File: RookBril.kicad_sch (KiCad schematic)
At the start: 29 parts, among them J2 IR_SENSOR0_PINS, J3 IR_SENSOR1_PINS, J4 IR_SENSOR2_PINS, J5 IR_SENSOR3_PINS, J6 LOW-BAT_LED_CONN, J7 PDLC_JST_PINS, U1 VNH7070ASTR

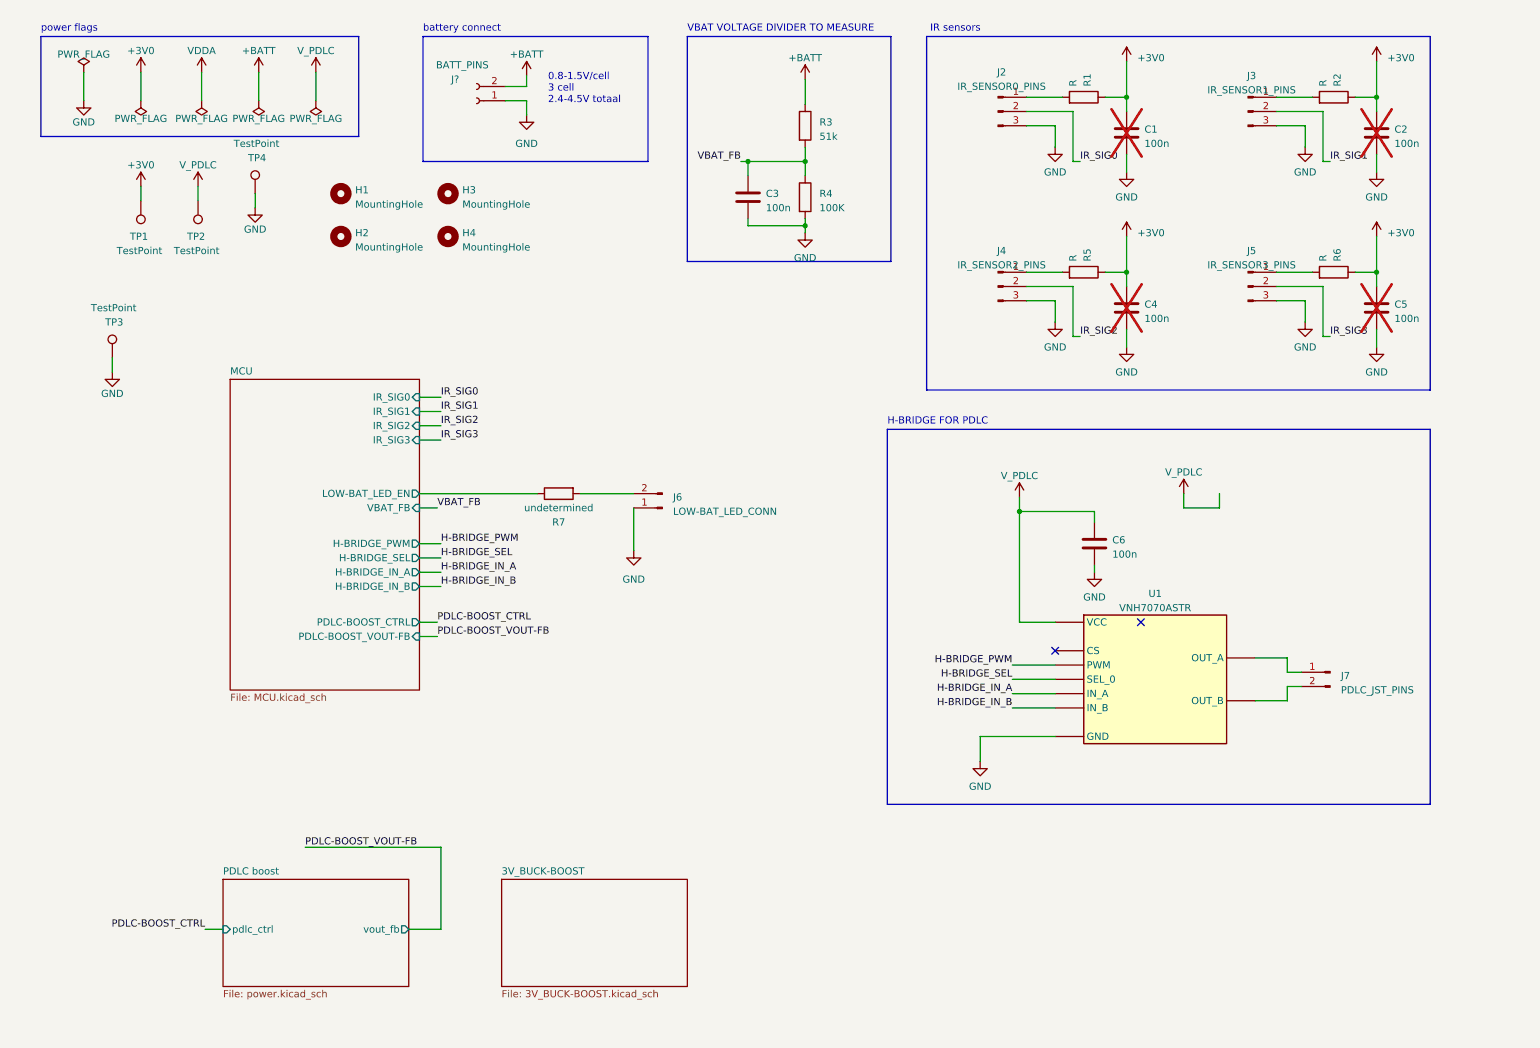
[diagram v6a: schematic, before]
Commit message: PCBv2.01
Eerste versie van de tweede versie van de pcb prototype.
Nieuwe PDLC voeding, extra pinnen beschikbaar voor GUI inclusief voeding pinnen.
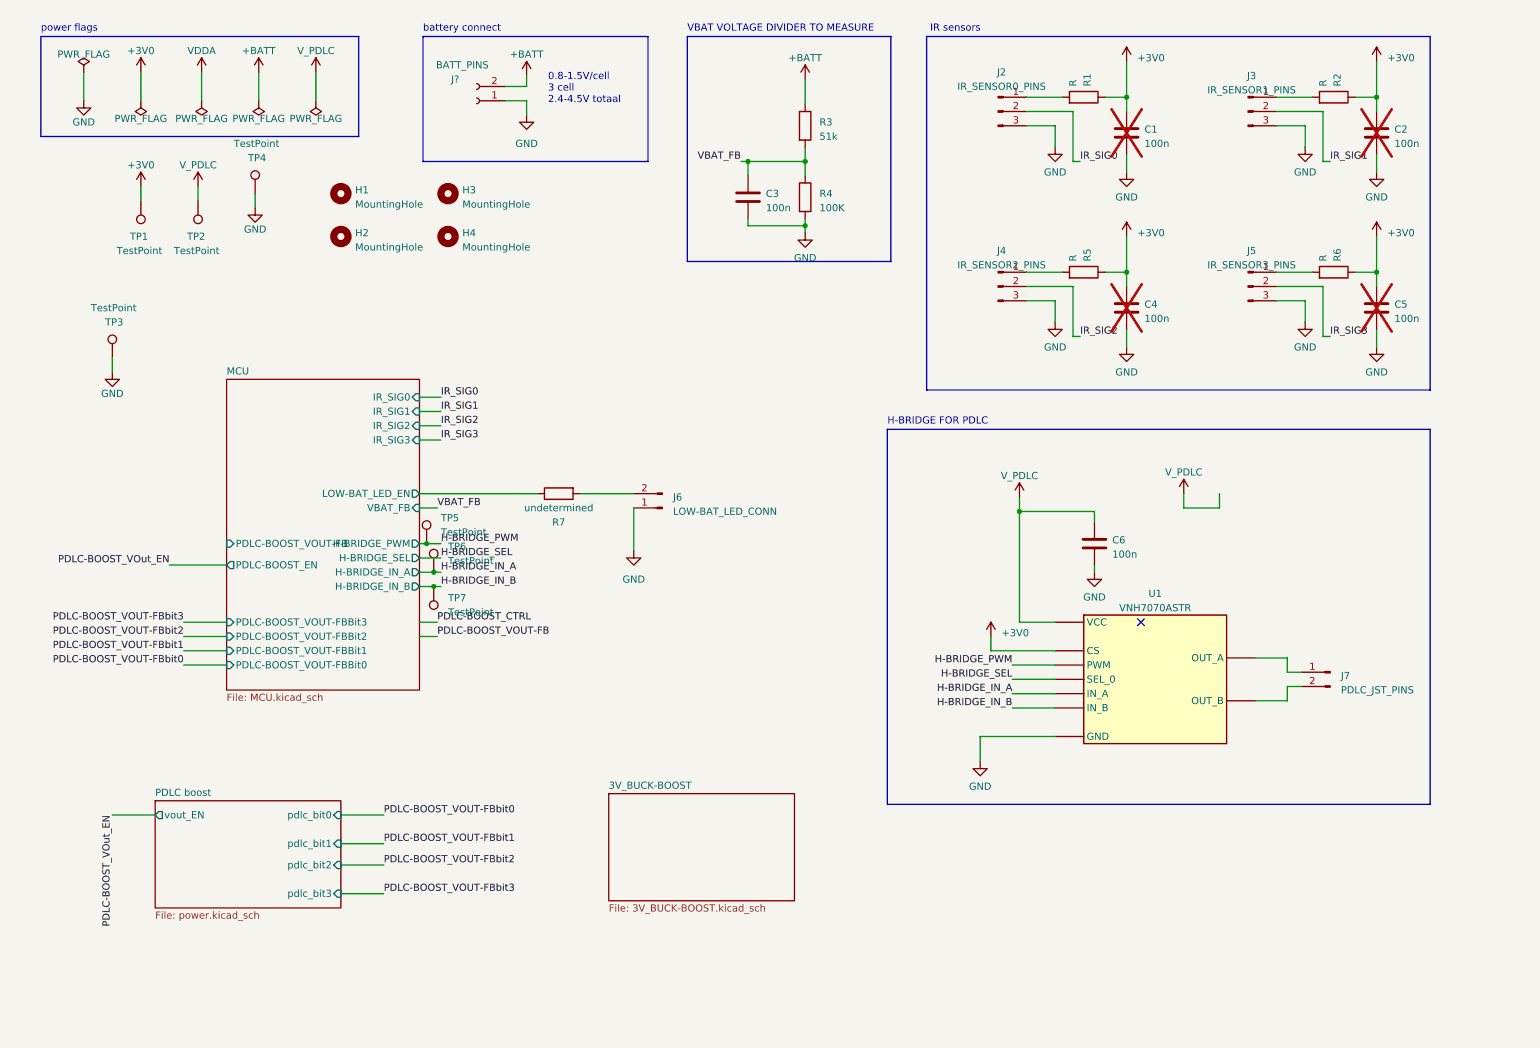
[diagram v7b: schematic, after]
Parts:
- added TP5, TP6, TP7: TestPoint, TestPoint:TestPoint_Pad_D1.0mm, symbol Connector:TestPoint
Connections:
- net +3V0: now also U1.13 (CS)
- net H-BRIDGE_IN_A: now also TP6.1
- net H-BRIDGE_IN_B: now also TP7.1
- net H-BRIDGE_PWM: now also TP5.1
- no-connect marks 2 -> 1
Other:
- sheet MCU ports: added PDLC-BOOST_EN, PDLC-BOOST_VOUT-FBBit0, PDLC-BOOST_VOUT-FBBit1, PDLC-BOOST_VOUT-FBBit2, PDLC-BOOST_VOUT-FBBit3; removed PDLC-BOOST_CTRL
- sheet PDLC boost ports: added pdlc_bit0, pdlc_bit1, pdlc_bit2, pdlc_bit3, vout_EN; removed pdlc_ctrl, vout_fb

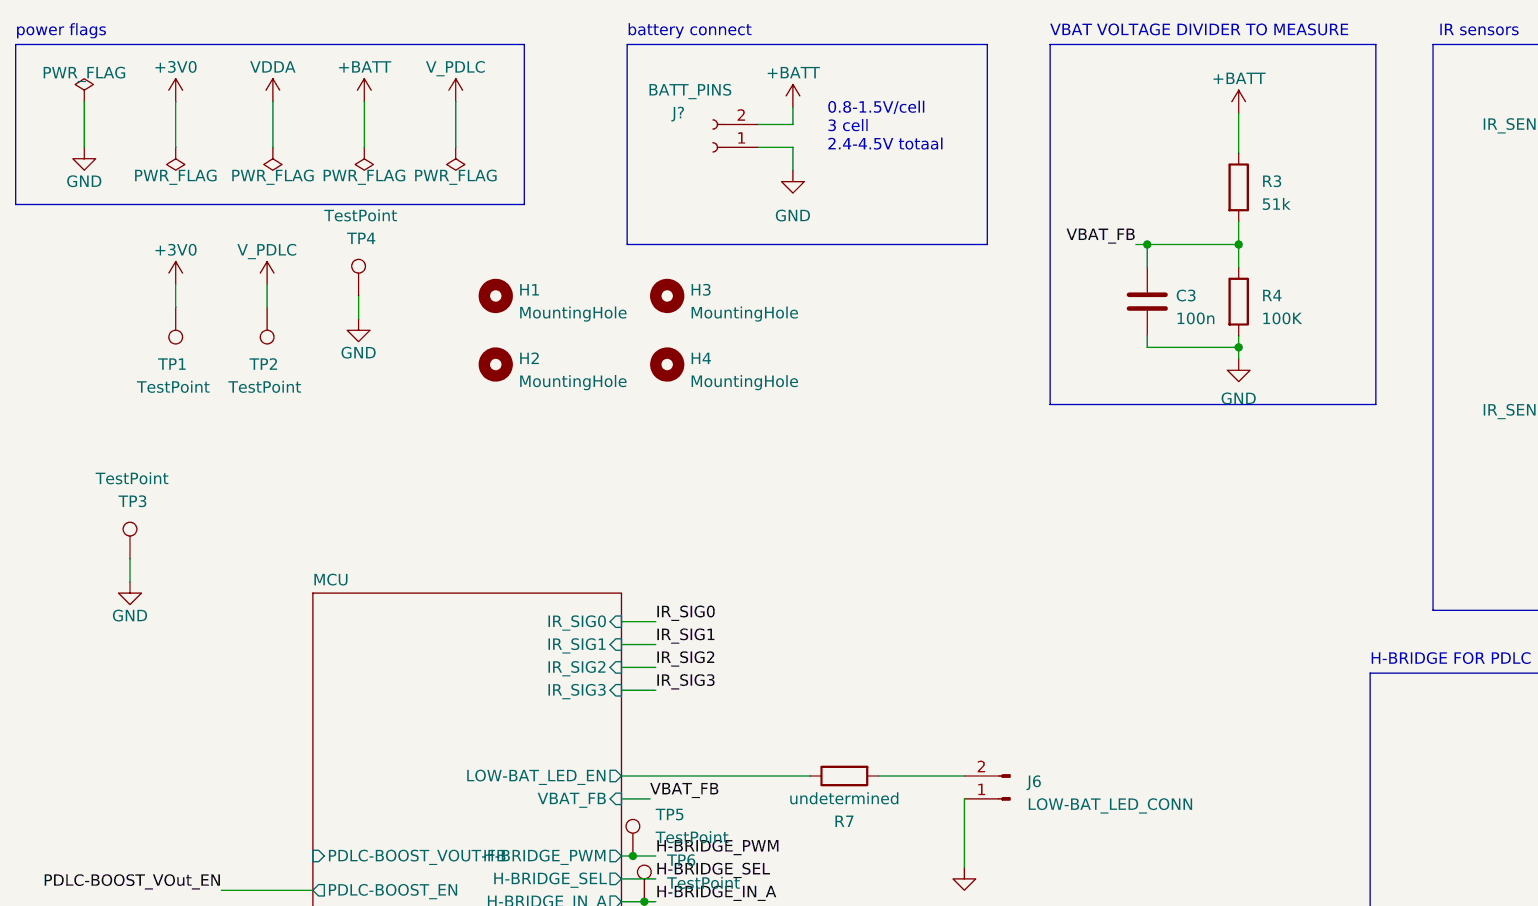
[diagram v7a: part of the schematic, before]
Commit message: PCBv2.02
Toepassingen van wouters feedback.
Condensatoren beter geplaatst bij pdlc, mosfet toegevoegd bij fb bat, extra vias toegevoegd en traces verschoven voor betere GND plane connecties
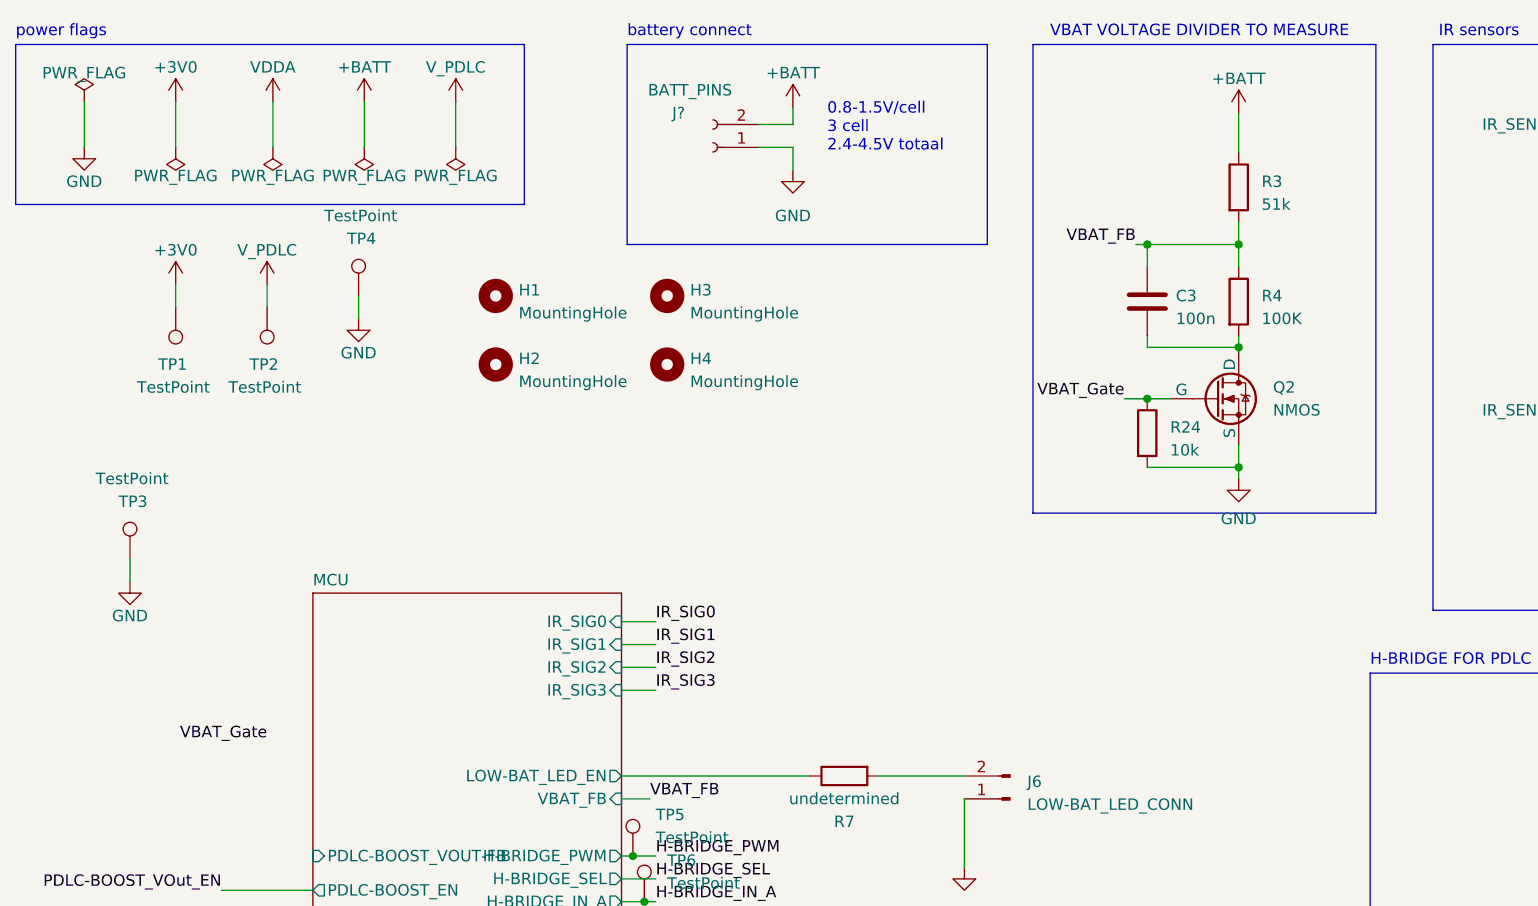
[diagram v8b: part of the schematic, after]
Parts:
- added Q2: NMOS, Package_TO_SOT_SMD:SOT-23, symbol Simulation_SPICE:NMOS
- added R24: 10k, Resistor_SMD:R_0805_2012Metric_Pad1.20x1.40mm_HandSolder, symbol Device:R
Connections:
- net GND: now also Q2.3 (S), R24.2; no longer C3.2, R4.2
- new net: C3.2, Q2.1 (D), R4.2
- new net VBAT_Gate: Q2.2 (G), R24.1
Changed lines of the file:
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@@
   (junction (at 151.13 51.435) (diameter 0) (color 0 0 0 0)
   )
+  (junction (at 140.97 57.15) (diameter 0) (color 0 0 0 0)
+  )
   (junction (at 140.97 40.005) (diameter 0) (color 0 0 0 0)
   )
@@
   )
   (junction (at 85.09 115.57) (diameter 0) (color 0 0 0 0)
+  )
+  (junction (at 151.13 64.77) (diameter 0) (color 0 0 0 0)
   )
   (junction (at 85.09 113.03) (diameter 0) (color 0 0 0 0)
@@
     (stroke (width 0) (type default))
   )
+  (wire (pts (xy 138.43 57.15) (xy 140.97 57.15))
+    (stroke (width 0) (type default))
+  )
   (wire (pts (xy 243.205 40.005) (xy 244.475 40.005))
     (stroke (width 0) (type default))
@@
     (stroke (width 0) (type default))
   )
+  (wire (pts (xy 140.97 57.15) (xy 143.51 57.15))
+    (stroke (width 0) (type default))
+  )
   (wire (pts (xy 243.205 31.115) (xy 234.95 31.115))
     (stroke (width 0) (type default))
@@
     (stroke (width 0) (type default))
   )
+  (wire (pts (xy 151.13 64.77) (xy 151.13 62.23))
+    (stroke (width 0) (type default))
+  )
   (wire (pts (xy 224.79 101.6) (xy 224.79 99.06))
     (stroke (width 0) (type default))
@@
     (stroke (width 0) (type default))
   )
+  (wire (pts (xy 140.97 64.77) (xy 151.13 64.77))
+    (stroke (width 0) (type default))
+  )
   (wire (pts (xy 184.15 124.46) (xy 184.15 127))
     (stroke (width 0) (type default))
@@
     (stroke (width 0) (type default))
   )
-  (wire (pts (xy 151.13 52.705) (xy 151.13 51.435))
+  (wire (pts (xy 151.13 66.04) (xy 151.13 64.77))
     (stroke (width 0) (type default))
   )
@@
     (stroke (width 0) (type default))
   )
+  (wire (pts (xy 151.13 52.07) (xy 151.13 51.435))
+    (stroke (width 0) (type default))
+  )
   (rectangle (start 83.185 17.78) (end 123.19 40.005)
     (stroke (width 0) (type default))
@@
     (fill (type none))
   )
-  (rectangle (start 130.175 17.78) (end 166.37 57.785)
+  (rectangle (start 128.27 17.78) (end 166.37 69.85)
     (stroke (width 0) (type default))
     (fill (type none))
@@
     (effects (font (size 1.27 1.27)) (justify left bottom))
   )
+  (label "VBAT_Gate" (at 138.43 57.15 180) (fields_autoplaced)
+    (effects (font (size 1.27 1.27)) (justify right bottom))
+  )
   (label "VBAT_FB" (at 139.7 40.005 180) (fields_autoplaced)
     (effects (font (size 1.27 1.27)) (justify right bottom))
@@
   (label "IR_SIG0" (at 200.025 40.005 0) (fields_autoplaced)
     (effects (font (size 1.27 1.27)) (justify left bottom))
+  )
+  (label "VBAT_Gate" (at 43.18 95.25 180) (fields_autoplaced)
+    (effects (font (size 1.27 1.27)) (justify right bottom))
   )
   (label "IR_SIG0" (at 86.36 81.915 0) (fields_autoplaced)
@@
     )
   )
+  (symbol (lib_id "Device:R") (at 140.97 60.96 0) (unit 1)
+    (in_bom yes) (on_board yes) (dnp no) (fields_autoplaced)
+    (property "Reference" "R24" (at 143.51 60.325 0)
+      (effects (font (size 1.27 1.27)) (justify left))
+    )
+    (property "Value" "10k" (at 143.51 62.865 0)
+      (effects (font (size 1.27 1.27)) (justify left))
+    )
+    (property "Footprint" "Resistor_SMD:R_0805_2012Metric_Pad1.20x1.40mm_HandSolder" (at 139.192 60.96 90)
+      (effects (font (size 1.27 1.27)) hide)
+    )
+    (property "Datasheet" "~" (at 140.97 60.96 0)
+      (effects (font (size 1.27 1.27)) hide)
+    )
+    (pin "1")
+    (pin "2")
+    (instances
+      (project "RookBril"
+        (path "/5dc439a9-720d-4bdc-b61f-78a76fde4df5"
+          (reference "R24") (unit 1)
+        )
+      )
+    )
+  )
   (symbol (lib_id "Mechanical:MountingHole") (at 87.63 53.34 0) (unit 1)
     (in_bom yes) (on_board yes) (dnp no) (fields_autoplaced)
@@
         (path "/5dc439a9-720d-4bdc-b61f-78a76fde4df5"
           (reference "TP6") (unit 1)
+        )
+      )
+    )
+  )
+  (symbol (lib_id "Simulation_SPICE:NMOS") (at 148.59 57.15 0) (unit 1)
+    (in_bom yes) (on_board yes) (dnp no) (fields_autoplaced)
+    (property "Reference" "Q2" (at 154.94 55.88 0)
+      (effects (font (size 1.27 1.27)) (justify left))
+    )
+    (property "Value" "NMOS" (at 154.94 58.42 0)
+      (effects (font (size 1.27 1.27)) (justify left))
+    )
+    (property "Footprint" "Package_TO_SOT_SMD:SOT-23" (at 153.67 54.61 0)
+      (effects (font (size 1.27 1.27)) hide)
+    )
+    (property "Datasheet" "https://ngspice.sourceforge.io/docs/ngspice-manual.pdf" (at 148.59 69.85 0)
+      (effects (font (size 1.27 1.27)) hide)
+    )
+    (property "Sim.Device" "NMOS" (at 148.59 74.295 0)
+      (effects (font (size 1.27 1.27)) hide)
+    )
+    (property "Sim.Type" "VDMOS" (at 148.59 76.2 0)
+      (effects (font (size 1.27 1.27)) hide)
+    )
+    (property "Sim.Pins" "1=D 2=G 3=S" (at 148.59 72.39 0)
+      (effects (font (size 1.27 1.27)) hide)
+    )
+    (pin "1")
+    (pin "3")
+    (pin "2")
+    (instances
+      (project "RookBril"
+        (path "/5dc439a9-720d-4bdc-b61f-78a76fde4df5/2d26b15a-54d8-4f7d-a410-dc25ffe321a1"
+          (reference "Q2") (unit 1)
+        )
+        (path "/5dc439a9-720d-4bdc-b61f-78a76fde4df5"
+          (reference "Q6") (unit 1)
         )
       )
@@
     )
   )
-  (symbol (lib_id "power:GND") (at 151.13 52.705 0) (unit 1)
-    (in_bom yes) (on_board yes) (dnp no) (fields_autoplaced)
-    (property "Reference" "#PWR015" (at 151.13 59.055 0)
-      (effects (font (size 1.27 1.27)) hide)
-    )
-    (property "Value" "GND" (at 151.13 57.15 0)
-      (effects (font (size 1.27 1.27)))
-    )
-    (property "Footprint" "" (at 151.13 52.705 0)
-      (effects (font (size 1.27 1.27)) hide)
-    )
-    (property "Datasheet" "" (at 151.13 52.705 0)
-      (effects (font (size 1.27 1.27)) hide)
-    )
+  (symbol (lib_id "power:GND") (at 151.13 66.04 0) (unit 1)
+    (in_bom yes) (on_board yes) (dnp no) (fields_autoplaced)
+    (property "Reference" "#PWR015" (at 151.13 72.39 0)
+      (effects (font (size 1.27 1.27)) hide)
+    )
+    (property "Value" "GND" (at 151.13 70.485 0)
+      (effects (font (size 1.27 1.27)))
+    )
+    (property "Footprint" "" (at 151.13 66.04 0)
+      (effects (font (size 1.27 1.27)) hide)
+    )
+    (property "Datasheet" "" (at 151.13 66.04 0)
+      (effects (font (size 1.27 1.27)) hide)
+    )
